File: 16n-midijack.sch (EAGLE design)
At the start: 108 parts, among them J1 PJ302M, J10 PJ302M, J11 PJ302M, J12 PJ302M, J13 PJ302M, J14 PJ302M, J15 PJ302M, J16 PJ302M, J2 PJ302M, J3 PJ302M, J4 PJ302M, J5 PJ302M, J6 PJ302M, J7 PJ302M, J8 PJ302M, J9 PJ302M, U1 MCP6004_SMD, U2 MCP6004_SMD, U3 MCP6004_SMD, U4 MCP6004_SMD, U5 MCP6004_SMD, U6 MCP6004_SMD, U7 MCP6004_SMD, U8 MCP6004_SMD

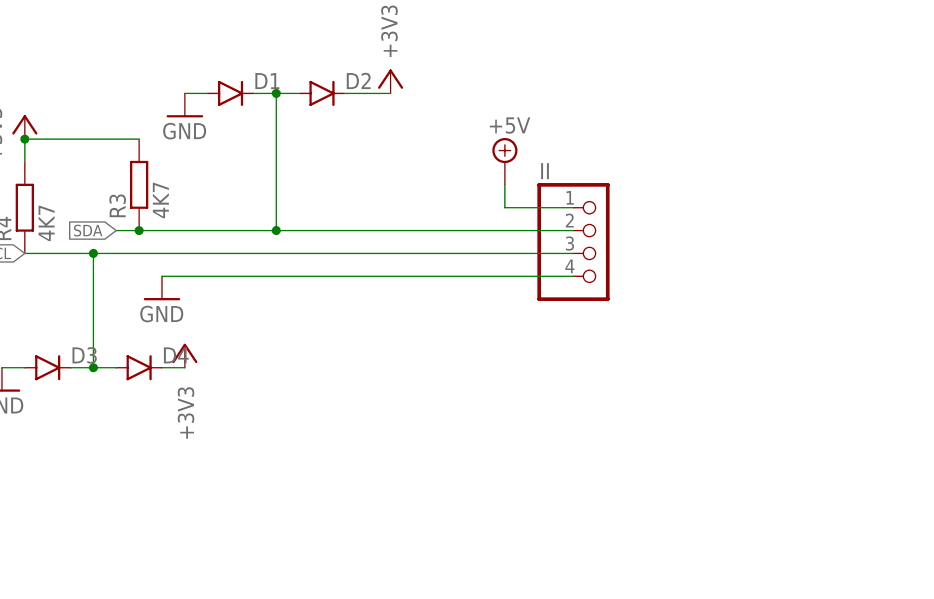
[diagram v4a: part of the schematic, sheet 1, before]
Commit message: Add 2x8 header for I2C; add fiducials.
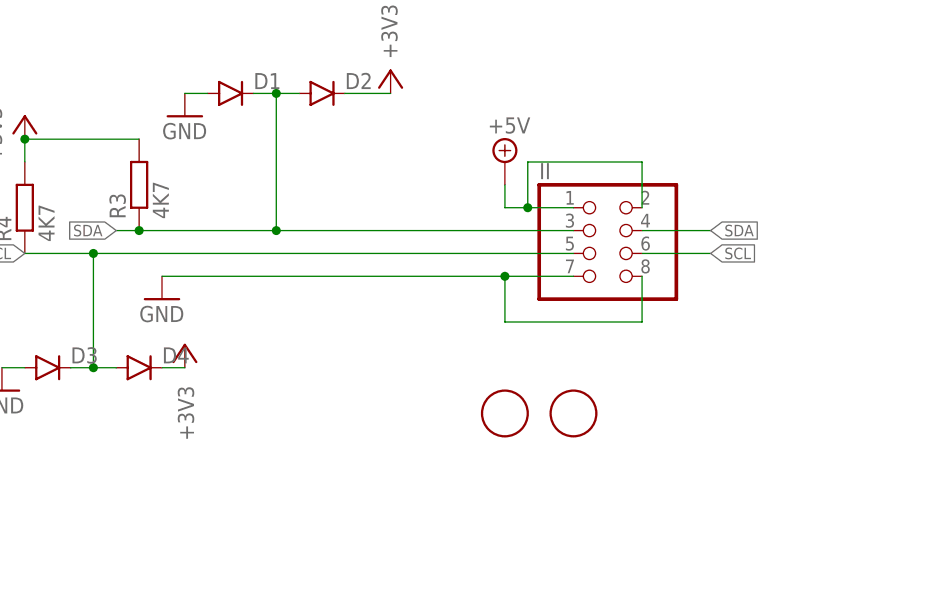
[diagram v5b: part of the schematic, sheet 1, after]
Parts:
- added FID1, FID2: FIDUCIAL, adafruit:FIDUCIAL
- II: device pinhead:PINHD-1X4/90 -> pinhead:PINHD-2X4/90
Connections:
- net +5V: now also II.2
- net GND: now also II.7, II.8; no longer II.4
- net SCL: now also II.5, II.6; no longer II.3
- net SDA: now also II.3, II.4; no longer II.2
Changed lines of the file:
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@@
 <part name="GND17" library="supply1" deviceset="GND" device=""/>
 <part name="S1" library="SparkFun-Electromechanical" deviceset="SWITCH-DPDT" device="EG2211"/>
-<part name="II" library="pinhead" library_urn="urn:adsk.eagle:library:325" deviceset="PINHD-1X4" device="/90" package3d_urn="urn:adsk.eagle:package:22404/1"/>
 <part name="GND19" library="supply1" deviceset="GND" device=""/>
 <part name="+3V18" library="supply1" deviceset="+3V3" device=""/>
@@
 <part name="R52" library="rcl" library_urn="urn:adsk.eagle:library:334" deviceset="R-EU_" device="R0805" package3d_urn="urn:adsk.eagle:package:23553/2" value="1K"/>
 <part name="+3V1" library="supply1" deviceset="+3V3" device=""/>
+<part name="II" library="pinhead" library_urn="urn:adsk.eagle:library:325" deviceset="PINHD-2X4" device="/90" package3d_urn="urn:adsk.eagle:package:22465/2"/>
+<part name="FID1" library="adafruit" library_urn="urn:adsk.eagle:library:420" deviceset="FIDUCIAL" device=""/>
+<part name="FID2" library="adafruit" library_urn="urn:adsk.eagle:library:420" deviceset="FIDUCIAL" device=""/>
 </parts>
 <sheets>
@@
 <instance part="GND17" gate="1" x="190.5" y="126.746" rot="R180"/>
 <instance part="S1" gate="G$1" x="205.74" y="116.84"/>
-<instance part="II" gate="A" x="325.12" y="109.22"/>
 <instance part="GND19" gate="1" x="276.86" y="104.14"/>
 <instance part="+3V18" gate="G$1" x="261.62" y="124.46"/>
@@
 <instance part="SUPPLY33" gate="GND" x="353.06" y="203.2"/>
 <instance part="+3V1" gate="G$1" x="241.3" y="119.38"/>
+<instance part="II" gate="A" x="325.12" y="109.22"/>
+<instance part="FID1" gate="G$1" x="314.96" y="91.44"/>
+<instance part="FID2" gate="G$1" x="322.58" y="91.44"/>
 </instances>
 <busses>
@@
 </segment>
 <segment>
-<pinref part="II" gate="A" pin="4"/>
-<wire x1="322.58" y1="106.68" x2="276.86" y2="106.68" width="0.1524" layer="91"/>
+<wire x1="322.58" y1="106.68" x2="314.96" y2="106.68" width="0.1524" layer="91"/>
 <pinref part="GND19" gate="1" pin="GND"/>
+<pinref part="II" gate="A" pin="7"/>
+<wire x1="314.96" y1="106.68" x2="276.86" y2="106.68" width="0.1524" layer="91"/>
+<wire x1="314.96" y1="106.68" x2="314.96" y2="101.6" width="0.1524" layer="91"/>
+<junction x="314.96" y="106.68"/>
+<pinref part="II" gate="A" pin="8"/>
+<wire x1="314.96" y1="101.6" x2="330.2" y2="101.6" width="0.1524" layer="91"/>
+<wire x1="330.2" y1="101.6" x2="330.2" y2="106.68" width="0.1524" layer="91"/>
 </segment>
 <segment>
@@
 </segment>
 <segment>
+<wire x1="322.58" y1="114.3" x2="317.5" y2="114.3" width="0.1524" layer="91"/>
+<pinref part="SUPPLY1" gate="+5V" pin="+5V"/>
+<wire x1="317.5" y1="114.3" x2="314.96" y2="114.3" width="0.1524" layer="91"/>
+<wire x1="314.96" y1="116.84" x2="314.96" y2="114.3" width="0.1524" layer="91"/>
 <pinref part="II" gate="A" pin="1"/>
-<wire x1="322.58" y1="114.3" x2="314.96" y2="114.3" width="0.1524" layer="91"/>
-<pinref part="SUPPLY1" gate="+5V" pin="+5V"/>
-<wire x1="314.96" y1="116.84" x2="314.96" y2="114.3" width="0.1524" layer="91"/>
+<pinref part="II" gate="A" pin="2"/>
+<wire x1="330.2" y1="114.3" x2="330.2" y2="116.84" width="0.1524" layer="91"/>
+<wire x1="330.2" y1="116.84" x2="330.2" y2="119.38" width="0.1524" layer="91"/>
+<wire x1="330.2" y1="119.38" x2="317.5" y2="119.38" width="0.1524" layer="91"/>
+<wire x1="317.5" y1="119.38" x2="317.5" y2="114.3" width="0.1524" layer="91"/>
+<junction x="317.5" y="114.3"/>
 </segment>
 <segment>
@@
 <net name="SDA" class="0">
 <segment>
-<pinref part="II" gate="A" pin="2"/>
 <wire x1="322.58" y1="111.76" x2="289.56" y2="111.76" width="0.1524" layer="91"/>
 <label x="271.78" y="111.76" size="1.27" layer="95" rot="R180" xref="yes"/>
@@
 <junction x="289.56" y="127"/>
 <junction x="289.56" y="111.76"/>
+<pinref part="II" gate="A" pin="3"/>
 </segment>
 <segment>
@@
 <label x="129.54" y="88.9" size="1.778" layer="95"/>
 </segment>
+<segment>
+<pinref part="II" gate="A" pin="4"/>
+<wire x1="330.2" y1="111.76" x2="337.82" y2="111.76" width="0.1524" layer="91"/>
+<label x="337.82" y="111.76" size="1.27" layer="95" xref="yes"/>
+</segment>
 </net>
 <net name="SCL" class="0">
 <segment>
-<pinref part="II" gate="A" pin="3"/>
 <wire x1="322.58" y1="109.22" x2="269.24" y2="109.22" width="0.1524" layer="91"/>
 <label x="261.62" y="109.22" size="1.27" layer="95" rot="R180" xref="yes"/>
@@
 <junction x="269.24" y="96.52"/>
 <junction x="269.24" y="109.22"/>
+<pinref part="II" gate="A" pin="5"/>
 </segment>
 <segment>
@@
 <label x="129.54" y="86.36" size="1.778" layer="95"/>
 </segment>
-</net>
+<segment>
+<pinref part="II" gate="A" pin="6"/>
+<wire x1="330.2" y1="109.22" x2="337.82" y2="109.22" width="0.1524" layer="91"/>
+<label x="337.82" y="109.22" size="1.27" layer="95" xref="yes"/>
+</segment>
+</net>

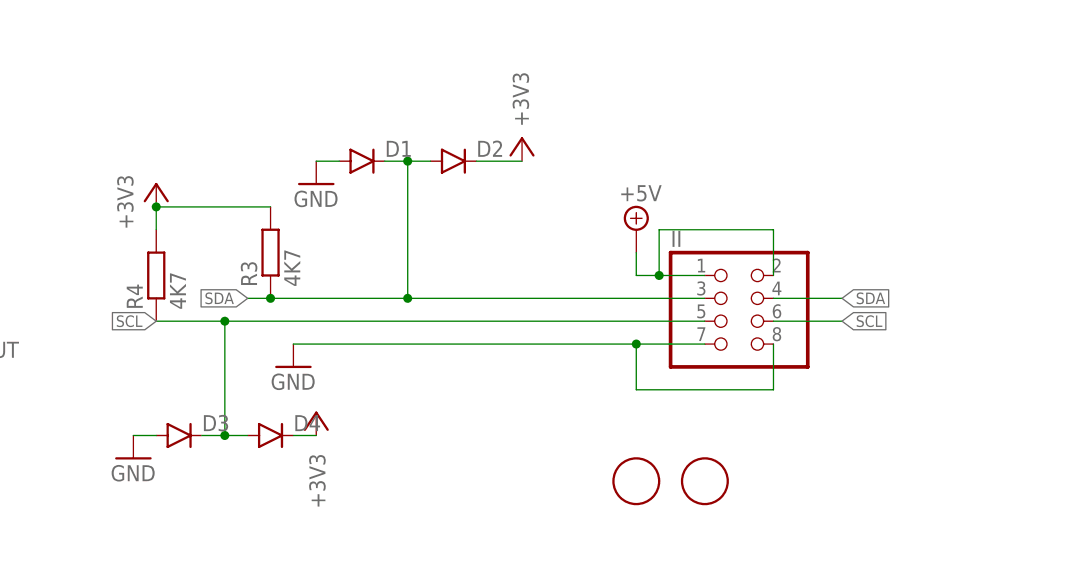
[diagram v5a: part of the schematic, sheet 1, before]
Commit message: Move II to TRS; label II and MIDI jacks.
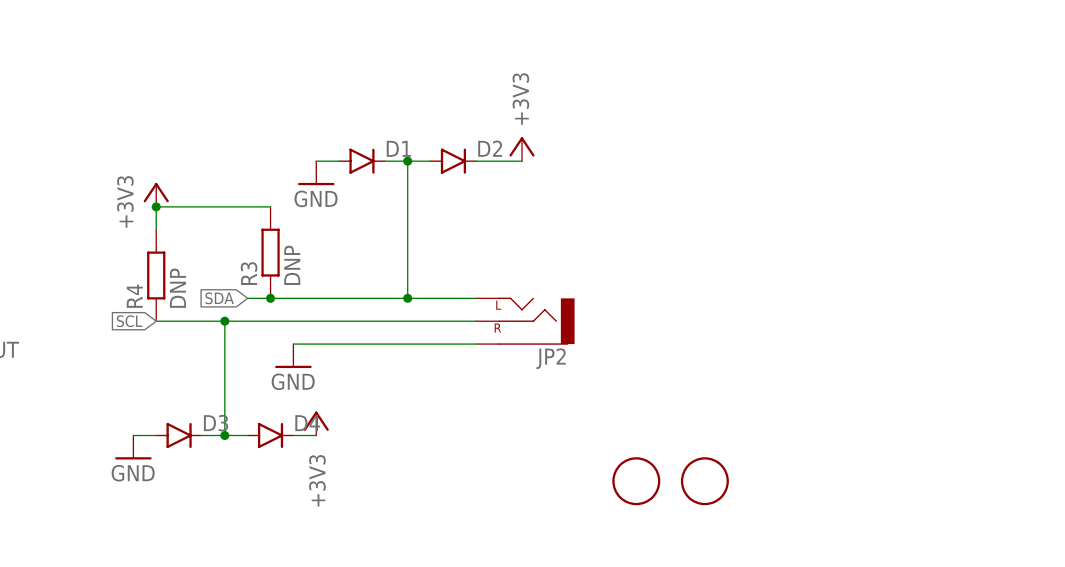
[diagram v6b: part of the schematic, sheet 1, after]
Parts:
- removed II: (no value), pinhead:PINHD-2X4/90
- added JP2: (no value), SparkFun-Connectors:AUDIO-JACKPTH
- R3, R4: value 4K7 -> DNP
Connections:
- net +5V: no longer II.1, II.2
- net GND: now also JP2.SLEEVE; no longer II.7, II.8
- net SCL: now also JP2.RIGHT; no longer II.5, II.6
- net SDA: now also JP2.LEFT; no longer II.3, II.4
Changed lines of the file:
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@@
 <?xml version="1.0" encoding="utf-8"?>
 <!DOCTYPE eagle SYSTEM "eagle.dtd">
-<eagle version="8.4.3">
+<eagle version="8.5.0">
 <drawing>
 <settings>
@@
 <part name="GND19" library="supply1" deviceset="GND" device=""/>
 <part name="+3V18" library="supply1" deviceset="+3V3" device=""/>
-<part name="R3" library="rcl" library_urn="urn:adsk.eagle:library:334" deviceset="R-EU_" device="R0805" package3d_urn="urn:adsk.eagle:package:23553/2" value="4K7"/>
-<part name="R4" library="rcl" library_urn="urn:adsk.eagle:library:334" deviceset="R-EU_" device="R0805" package3d_urn="urn:adsk.eagle:package:23553/2" value="4K7"/>
+<part name="R3" library="rcl" library_urn="urn:adsk.eagle:library:334" deviceset="R-EU_" device="R0805" package3d_urn="urn:adsk.eagle:package:23553/2" value="DNP"/>
+<part name="R4" library="rcl" library_urn="urn:adsk.eagle:library:334" deviceset="R-EU_" device="R0805" package3d_urn="urn:adsk.eagle:package:23553/2" value="DNP"/>
 <part name="D1" library="foxfield" deviceset="DIODE" device="SOD123" value=""/>
 <part name="D2" library="foxfield" deviceset="DIODE" device="SOD123" value=""/>
@@
 <part name="+3V20" library="supply1" deviceset="+3V3" device=""/>
 <part name="+3V21" library="supply1" deviceset="+3V3" device=""/>
-<part name="SUPPLY1" library="supply2" library_urn="urn:adsk.eagle:library:372" deviceset="+5V" device=""/>
 <part name="SUPPLY2" library="supply2" library_urn="urn:adsk.eagle:library:372" deviceset="+5V" device=""/>
 <part name="SUPPLY3" library="supply2" library_urn="urn:adsk.eagle:library:372" deviceset="+5V" device=""/>
@@
 <part name="R52" library="rcl" library_urn="urn:adsk.eagle:library:334" deviceset="R-EU_" device="R0805" package3d_urn="urn:adsk.eagle:package:23553/2" value="1K"/>
 <part name="+3V1" library="supply1" deviceset="+3V3" device=""/>
-<part name="II" library="pinhead" library_urn="urn:adsk.eagle:library:325" deviceset="PINHD-2X4" device="/90" package3d_urn="urn:adsk.eagle:package:22465/2"/>
 <part name="FID1" library="adafruit" library_urn="urn:adsk.eagle:library:420" deviceset="FIDUCIAL" device=""/>
 <part name="FID2" library="adafruit" library_urn="urn:adsk.eagle:library:420" deviceset="FIDUCIAL" device=""/>
+<part name="JP2" library="SparkFun-Connectors" deviceset="AUDIO-JACK" device="PTH"/>
 </parts>
 <sheets>
@@
 <attribute name="VALUE" x="280.416" y="88.392" size="1.778" layer="96" rot="R90"/>
 </instance>
-<instance part="SUPPLY1" gate="+5V" x="314.96" y="119.38"/>
 <instance part="SUPPLY2" gate="+5V" x="53.34" y="190.5"/>
 <instance part="SUPPLY3" gate="+5V" x="73.66" y="190.5"/>
@@
 <instance part="SUPPLY33" gate="GND" x="353.06" y="203.2"/>
 <instance part="+3V1" gate="G$1" x="241.3" y="119.38"/>
-<instance part="II" gate="A" x="325.12" y="109.22"/>
 <instance part="FID1" gate="G$1" x="314.96" y="91.44"/>
 <instance part="FID2" gate="G$1" x="322.58" y="91.44"/>
+<instance part="JP2" gate="G$1" x="302.26" y="109.22" rot="R180"/>
 </instances>
 <busses>
@@
 </segment>
 <segment>
-<wire x1="322.58" y1="106.68" x2="314.96" y2="106.68" width="0.1524" layer="91"/>
 <pinref part="GND19" gate="1" pin="GND"/>
-<pinref part="II" gate="A" pin="7"/>
-<wire x1="314.96" y1="106.68" x2="276.86" y2="106.68" width="0.1524" layer="91"/>
-<wire x1="314.96" y1="106.68" x2="314.96" y2="101.6" width="0.1524" layer="91"/>
-<junction x="314.96" y="106.68"/>
-<pinref part="II" gate="A" pin="8"/>
-<wire x1="314.96" y1="101.6" x2="330.2" y2="101.6" width="0.1524" layer="91"/>
-<wire x1="330.2" y1="101.6" x2="330.2" y2="106.68" width="0.1524" layer="91"/>
+<wire x1="297.18" y1="106.68" x2="276.86" y2="106.68" width="0.1524" layer="91"/>
+<pinref part="JP2" gate="G$1" pin="SLEEVE"/>
 </segment>
 <segment>
@@
 <wire x1="127" y1="139.7" x2="127" y2="147.32" width="0.1524" layer="91"/>
 <label x="126.238" y="142.24" size="1.778" layer="95" rot="R90"/>
-</segment>
-<segment>
-<wire x1="322.58" y1="114.3" x2="317.5" y2="114.3" width="0.1524" layer="91"/>
-<pinref part="SUPPLY1" gate="+5V" pin="+5V"/>
-<wire x1="317.5" y1="114.3" x2="314.96" y2="114.3" width="0.1524" layer="91"/>
-<wire x1="314.96" y1="116.84" x2="314.96" y2="114.3" width="0.1524" layer="91"/>
-<pinref part="II" gate="A" pin="1"/>
-<pinref part="II" gate="A" pin="2"/>
-<wire x1="330.2" y1="114.3" x2="330.2" y2="116.84" width="0.1524" layer="91"/>
-<wire x1="330.2" y1="116.84" x2="330.2" y2="119.38" width="0.1524" layer="91"/>
-<wire x1="330.2" y1="119.38" x2="317.5" y2="119.38" width="0.1524" layer="91"/>
-<wire x1="317.5" y1="119.38" x2="317.5" y2="114.3" width="0.1524" layer="91"/>
-<junction x="317.5" y="114.3"/>
 </segment>
 <segment>
@@
 <net name="SDA" class="0">
 <segment>
-<wire x1="322.58" y1="111.76" x2="289.56" y2="111.76" width="0.1524" layer="91"/>
+<wire x1="297.18" y1="111.76" x2="289.56" y2="111.76" width="0.1524" layer="91"/>
 <label x="271.78" y="111.76" size="1.27" layer="95" rot="R180" xref="yes"/>
 <pinref part="R3" gate="G$1" pin="1"/>
@@
 <junction x="289.56" y="127"/>
 <junction x="289.56" y="111.76"/>
-<pinref part="II" gate="A" pin="3"/>
+<pinref part="JP2" gate="G$1" pin="LEFT"/>
 </segment>
 <segment>
@@
 <label x="129.54" y="88.9" size="1.778" layer="95"/>
 </segment>
-<segment>
-<pinref part="II" gate="A" pin="4"/>
-<wire x1="330.2" y1="111.76" x2="337.82" y2="111.76" width="0.1524" layer="91"/>
-<label x="337.82" y="111.76" size="1.27" layer="95" xref="yes"/>
-</segment>
 </net>
 <net name="SCL" class="0">
 <segment>
-<wire x1="322.58" y1="109.22" x2="269.24" y2="109.22" width="0.1524" layer="91"/>
+<wire x1="297.18" y1="109.22" x2="269.24" y2="109.22" width="0.1524" layer="91"/>
 <label x="261.62" y="109.22" size="1.27" layer="95" rot="R180" xref="yes"/>
 <pinref part="R4" gate="G$1" pin="1"/>
@@
 <junction x="269.24" y="96.52"/>
 <junction x="269.24" y="109.22"/>
-<pinref part="II" gate="A" pin="5"/>
+<pinref part="JP2" gate="G$1" pin="RIGHT"/>
 </segment>
 <segment>
@@
 <label x="129.54" y="86.36" size="1.778" layer="95"/>
 </segment>
-<segment>
-<pinref part="II" gate="A" pin="6"/>
-<wire x1="330.2" y1="109.22" x2="337.82" y2="109.22" width="0.1524" layer="91"/>
-<label x="337.82" y="109.22" size="1.27" layer="95" xref="yes"/>
-</segment>
-</net>
+</net>
